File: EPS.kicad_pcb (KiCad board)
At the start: 6 copper layers, 90.2 x 95.9 mm, 1 part

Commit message: progress on switch sheet
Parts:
- added C1101: 1uF, Capacitor_SMD:C_0603_1608Metric_Pad1.08x0.95mm_HandSolder, F.Cu at (64.4, 59.4)
- added C1102: 1uF, Capacitor_SMD:C_0603_1608Metric_Pad1.08x0.95mm_HandSolder, F.Cu at (64.7, 66.5)
- added C1103: 1uF, Capacitor_SMD:C_0603_1608Metric_Pad1.08x0.95mm_HandSolder, F.Cu at (67.7, 65.5)
- added C1104: 1uF, Capacitor_SMD:C_0603_1608Metric_Pad1.08x0.95mm_HandSolder, F.Cu at (67.7, 58.2)
- added C1105: 100nF, Capacitor_SMD:C_0603_1608Metric_Pad1.08x0.95mm_HandSolder, F.Cu at (64.4, 62.8)
- added C1106: 100nF, Capacitor_SMD:C_0603_1608Metric_Pad1.08x0.95mm_HandSolder, F.Cu at (64.6, 70.1)
- added C1301: 1uF, Capacitor_SMD:C_0603_1608Metric_Pad1.08x0.95mm_HandSolder, F.Cu at (41.0, 75.9)
- added C1302: 1uF, Capacitor_SMD:C_0603_1608Metric_Pad1.08x0.95mm_HandSolder, F.Cu at (41.0, 78.5)
- added C1303: 1uF, Capacitor_SMD:C_0603_1608Metric_Pad1.08x0.95mm_HandSolder, F.Cu at (41.0, 81.0)
- added C1304: 1uF, Capacitor_SMD:C_0603_1608Metric_Pad1.08x0.95mm_HandSolder, F.Cu at (41.0, 83.5)
- added C1305: 100nF, Capacitor_SMD:C_0603_1608Metric_Pad1.08x0.95mm_HandSolder, F.Cu at (41.0, 86.0)
- added C1306: 100nF, Capacitor_SMD:C_0603_1608Metric_Pad1.08x0.95mm_HandSolder, F.Cu at (41.0, 88.5)
- added C1601: 1uF, Capacitor_SMD:C_0603_1608Metric_Pad1.08x0.95mm_HandSolder, F.Cu at (53.5, 75.9)
- added C1602: 1uF, Capacitor_SMD:C_0603_1608Metric_Pad1.08x0.95mm_HandSolder, F.Cu at (53.5, 78.5)
- added C1603: 1uF, Capacitor_SMD:C_0603_1608Metric_Pad1.08x0.95mm_HandSolder, F.Cu at (53.5, 81.0)
- added C1604: 1uF, Capacitor_SMD:C_0603_1608Metric_Pad1.08x0.95mm_HandSolder, F.Cu at (53.5, 83.5)
- added C1605: 100nF, Capacitor_SMD:C_0603_1608Metric_Pad1.08x0.95mm_HandSolder, F.Cu at (53.5, 86.0)
- added C1606: 100nF, Capacitor_SMD:C_0603_1608Metric_Pad1.08x0.95mm_HandSolder, F.Cu at (53.5, 88.5)
- added C1701: 1uF, Capacitor_SMD:C_0603_1608Metric_Pad1.08x0.95mm_HandSolder, F.Cu at (53.5, 58.9)
- added C1702: 1uF, Capacitor_SMD:C_0603_1608Metric_Pad1.08x0.95mm_HandSolder, F.Cu at (53.5, 61.4)
- added C1703: 1uF, Capacitor_SMD:C_0603_1608Metric_Pad1.08x0.95mm_HandSolder, F.Cu at (53.5, 63.9)
- added C1704: 1uF, Capacitor_SMD:C_0603_1608Metric_Pad1.08x0.95mm_HandSolder, F.Cu at (53.5, 66.4)
- added C1705: 100nF, Capacitor_SMD:C_0603_1608Metric_Pad1.08x0.95mm_HandSolder, F.Cu at (53.5, 68.9)
- added C1706: 100nF, Capacitor_SMD:C_0603_1608Metric_Pad1.08x0.95mm_HandSolder, F.Cu at (53.5, 71.4)
- added C2801: 1uF, Capacitor_SMD:C_0603_1608Metric_Pad1.08x0.95mm_HandSolder, F.Cu at (41.0, 58.9)
- added C2802: 1uF, Capacitor_SMD:C_0603_1608Metric_Pad1.08x0.95mm_HandSolder, F.Cu at (41.0, 61.4)
- added C2803: 1uF, Capacitor_SMD:C_0603_1608Metric_Pad1.08x0.95mm_HandSolder, F.Cu at (41.0, 63.9)
- added C2804: 1uF, Capacitor_SMD:C_0603_1608Metric_Pad1.08x0.95mm_HandSolder, F.Cu at (41.0, 66.4)
- added C2805: 100nF, Capacitor_SMD:C_0603_1608Metric_Pad1.08x0.95mm_HandSolder, F.Cu at (41.0, 68.9)
- added C2806: 100nF, Capacitor_SMD:C_0603_1608Metric_Pad1.08x0.95mm_HandSolder, F.Cu at (41.0, 71.4)
- added U1101: MCP1703Ax-400xxMB, Package_TO_SOT_SMD:SOT-89-3, F.Cu at (68.3, 61.7)
- added U1102: MCP1703Ax-400xxMB, Package_TO_SOT_SMD:SOT-89-3, F.Cu at (68.5, 68.9)
- added U1301: MCP1703Ax-400xxMB, Package_TO_SOT_SMD:SOT-89-3, F.Cu at (46.5, 77.8)
- added U1302: MCP1703Ax-400xxMB, Package_TO_SOT_SMD:SOT-89-3, F.Cu at (46.5, 83.9)
- added U1601: MCP1703Ax-400xxMB, Package_TO_SOT_SMD:SOT-89-3, F.Cu at (59.0, 77.8)
- added U1602: MCP1703Ax-400xxMB, Package_TO_SOT_SMD:SOT-89-3, F.Cu at (59.0, 83.9)
- added U1701: MCP1703Ax-400xxMB, Package_TO_SOT_SMD:SOT-89-3, F.Cu at (59.0, 60.7)
- added U1702: MCP1703Ax-400xxMB, Package_TO_SOT_SMD:SOT-89-3, F.Cu at (59.0, 66.8)
- added U2801: MCP1703Ax-400xxMB, Package_TO_SOT_SMD:SOT-89-3, F.Cu at (46.5, 60.7)
- added U2802: MCP1703Ax-400xxMB, Package_TO_SOT_SMD:SOT-89-3, F.Cu at (46.5, 66.8)
- added U801: MSP430F5507IRGZ, Package_DFN_QFN:Texas_RGZ0048A_VQFN-48-1EP_7x7mm_P0.5mm_EP5.15x5.15mm, F.Cu at (68.3, 128.4)

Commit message: specified design
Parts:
- removed C1101, C1102, C1103, C1104, C1301, C1302, C1303, C1304, C1601, C1602, C1603, C1604, C1701, C1702, C1703, C1704, C2801, C2802, C2803, C2804: 1uF, Capacitor_SMD:C_0603_1608Metric_Pad1.08x0.95mm_HandSolder
- removed C1105, C1106, C1305, C1306, C1605, C1606, C1705, C1706, C2805, C2806: 100nF, Capacitor_SMD:C_0603_1608Metric_Pad1.08x0.95mm_HandSolder
- removed U1101, U1102, U1301, U1302, U1601, U1602, U1701, U1702, U2801, U2802: MCP1703Ax-400xxMB, Package_TO_SOT_SMD:SOT-89-3
- removed U801: MSP430F5507IRGZ, Package_DFN_QFN:Texas_RGZ0048A_VQFN-48-1EP_7x7mm_P0.5mm_EP5.15x5.15mm
- added H102: MountingHole, MountingHole:MountingHole_3.2mm_M3_Pad_Via, F.Cu at (160.0, 132.9)
- added H103: MountingHole, MountingHole:MountingHole_3.2mm_M3_Pad_Via, F.Cu at (240.0, 132.9)
- added H104: MountingHole, MountingHole:MountingHole_3.2mm_M3_Pad_Via, F.Cu at (163.9, 47.1)
- added H5901: Conn_02x26_Odd_Even, Connector_PinSocket_2.54mm:PinSocket_2x26_P2.54mm_Vertical, F.Cu at (168.9, 47.1)
- added H5902: Conn_02x26_Odd_Even, Connector_PinSocket_2.54mm:PinSocket_2x26_P2.54mm_Vertical, F.Cu at (168.9, 52.3)
- added PCB101: PCB Outline, Outlines:SPACEMANIC_V1c, F.Cu at (200.0, 90.0)
- added PCB102: PCB Outline, Outlines:SPACEMANIC_V1c, F.Cu at (84.6, 90.0)
- added PCB103: PCB Outline, Outlines:SPACEMANIC_V1c, F.Cu at (82.6, 200.1)
- added R_RX_5901: 0R, Resistor_SMD:R_0603_1608Metric_Pad0.98x0.95mm_HandSolder, F.Cu at (310.4, 164.3)
- added R_TX_5901: 0R, Resistor_SMD:R_0603_1608Metric_Pad0.98x0.95mm_HandSolder, F.Cu at (312.2, 164.3)
- H101: value PCB Outline -> MountingHole; footprint Outlines:SPACEMANIC_V1c -> MountingHole:MountingHole_3.2mm_M3_Pad_Via
- moved H101 103.0 mm to (237.5, 47.1)
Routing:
- net /Interface/RX: track 0.00 -> 4.78 mm
- net /Interface/RxD: track 0.00 -> 4.34 mm
- net /Interface/TX: track 0.00 -> 2.79 mm
- net /Interface/TxD: track 0.00 -> 2.39 mm
- added copper zone on In1.Cu, net GND
- added copper zone on In4.Cu, net GND
- added copper zone on B.Cu, net SHIELD
- added copper zone on F.Cu, net SHIELD
- added copper zone on In3.Cu, net VBUS
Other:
- board size 90.2 x 95.9 mm -> 90 x 95.8 mm

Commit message: added second AMUX and housekeeping
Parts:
- added H105: MountingHole, MountingHole:MountingHole_3.2mm_M3_Pad_Via, F.Cu at (48.5, 47.1)
- added H106: MountingHole, MountingHole:MountingHole_3.2mm_M3_Pad_Via, F.Cu at (44.6, 132.9)
- added H107: MountingHole, MountingHole:MountingHole_3.2mm_M3_Pad_Via, F.Cu at (124.6, 132.9)
- added H108: MountingHole, MountingHole:MountingHole_3.2mm_M3_Pad_Via, F.Cu at (122.1, 47.1)
- added PCB104: PCB Outline, Outlines:SPACEMANIC_V1c, F.Cu at (-181.4, 64.0)
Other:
- board size 90 x 95.8 mm -> 205.4 x 95.8 mm

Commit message: added RS422, housekeeping
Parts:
- moved PCB104 303.9 mm to (99.7, -51.3)
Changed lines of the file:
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@@
 	(footprint "Outlines:SPACEMANIC_V1c"
 		(layer "F.Cu")
-		(at -181.4075 64.05)
+		(at 99.7 -51.3)
 		(property "Reference" "PCB104"
 			(at 0 -0.5 0)

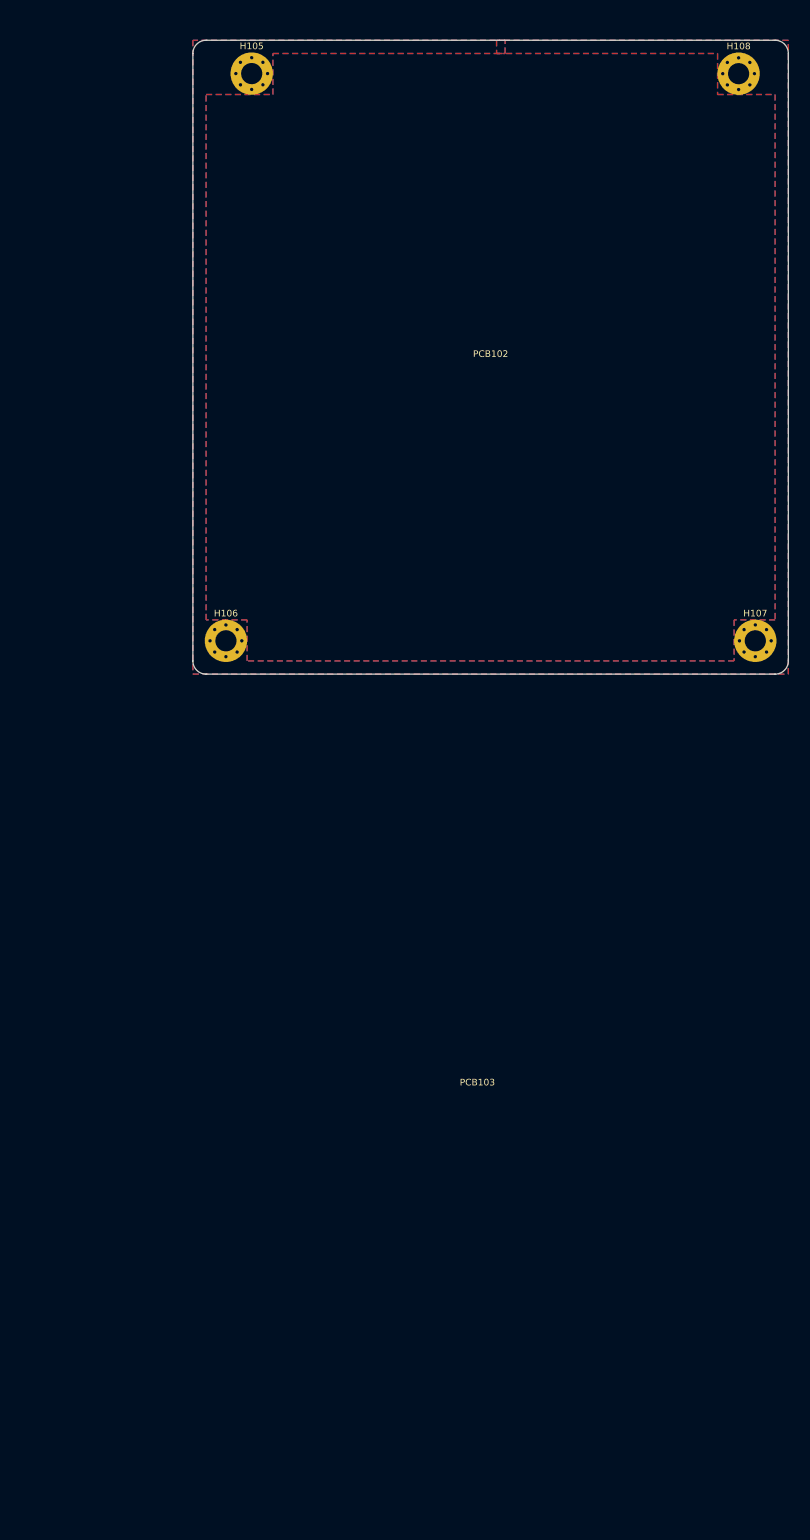
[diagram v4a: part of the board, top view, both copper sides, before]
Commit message: updated battery pack module; updated solar inputs module
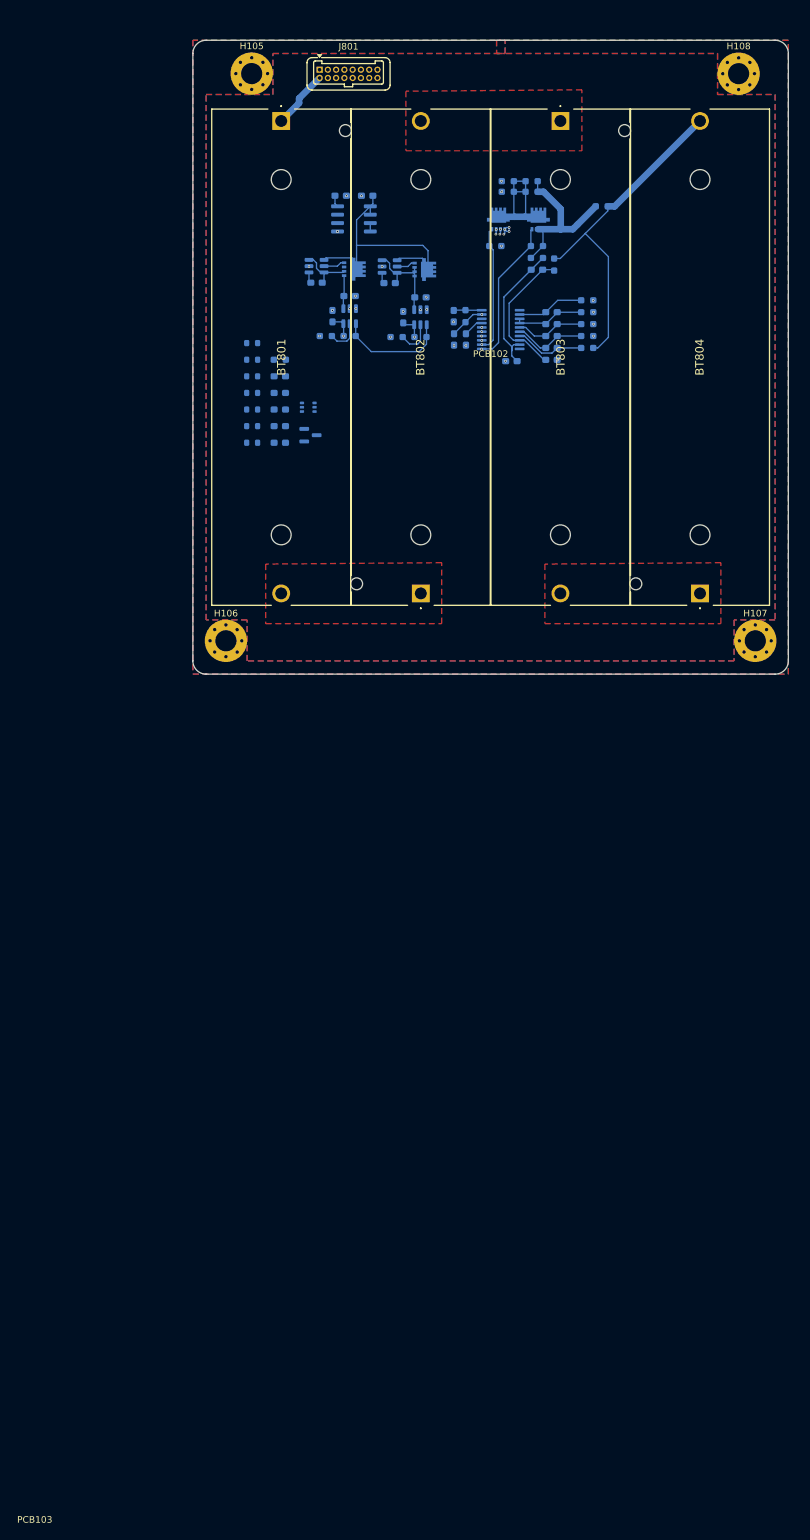
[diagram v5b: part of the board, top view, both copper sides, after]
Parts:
- added BT801: Battery_Cell, Outlines:BHC186501P-li-ion, F.Cu at (53.0, 54.3)
- added BT802: Battery_Cell, Outlines:BHC186501P-li-ion, F.Cu at (74.0, 125.7)
- added BT803: Battery_Cell, Outlines:BHC186501P-li-ion, F.Cu at (95.2, 54.3)
- added BT804: Battery_Cell, Outlines:BHC186501P-li-ion, F.Cu at (116.2, 125.7)
- added C2701: 1u, Capacitor_SMD:C_0603_1608Metric_Pad1.08x0.95mm_HandSolder, B.Cu at (52.7, 102.9)
- added C2702: 10n, Capacitor_SMD:C_0603_1608Metric_Pad1.08x0.95mm_HandSolder, B.Cu at (52.7, 100.4)
- added C2703: 10u, Capacitor_SMD:C_0603_1608Metric_Pad1.08x0.95mm_HandSolder, B.Cu at (52.7, 97.9)
- added C2704: 3.3n, Capacitor_SMD:C_0603_1608Metric_Pad1.08x0.95mm_HandSolder, B.Cu at (52.7, 95.4)
- added C2705: 10n, Capacitor_SMD:C_0603_1608Metric_Pad1.08x0.95mm_HandSolder, B.Cu at (52.7, 92.9)
- added C3301: 1u, Capacitor_SMD:C_0603_1608Metric_Pad1.08x0.95mm_HandSolder, B.Cu at (69.3, 78.8)
- added C3302: 1u, Capacitor_SMD:C_0603_1608Metric_Pad1.08x0.95mm_HandSolder, B.Cu at (58.3, 78.7)
- added C3303: 1u, Capacitor_SMD:C_0603_1608Metric_Pad1.08x0.95mm_HandSolder, B.Cu at (65.9, 65.6)
- added C3304: 1u, Capacitor_SMD:C_0603_1608Metric_Pad1.08x0.95mm_HandSolder, B.Cu at (61.9, 65.6)
- added C3501: 1u, Capacitor_SMD:C_0603_1608Metric_Pad1.08x0.95mm_HandSolder, B.Cu at (71.4, 84.0)
- added C3502: 1u, Capacitor_SMD:C_0603_1608Metric_Pad1.08x0.95mm_HandSolder, B.Cu at (60.7, 83.8)
- added C3503: 1u, Capacitor_SMD:C_0603_1608Metric_Pad1.08x0.95mm_HandSolder, B.Cu at (74.0, 81.0)
- added C3504: 1u, Capacitor_SMD:C_0603_1608Metric_Pad1.08x0.95mm_HandSolder, B.Cu at (63.3, 80.8)
- added C801: 1uF, Capacitor_SMD:C_0603_1608Metric_Pad1.08x0.95mm_HandSolder, B.Cu at (93.8, 83.2)
- added C802: 1uF, Capacitor_SMD:C_0603_1608Metric_Pad1.08x0.95mm_HandSolder, B.Cu at (93.8, 85.0)
- added C803: 1uF, Capacitor_SMD:C_0603_1608Metric_Pad1.08x0.95mm_HandSolder, B.Cu at (93.8, 86.8)
- added C804: 1uF, Capacitor_SMD:C_0603_1608Metric_Pad1.08x0.95mm_HandSolder, B.Cu at (93.8, 88.6)
- added C805: 1uF, Capacitor_SMD:C_0603_1608Metric_Pad1.08x0.95mm_HandSolder, B.Cu at (80.9, 87.3)
- added C806: C_Small, Capacitor_SMD:C_0603_1608Metric_Pad1.08x0.95mm_HandSolder, B.Cu at (79.1, 87.3)
- added C807: 1uF, Capacitor_SMD:C_0603_1608Metric_Pad1.08x0.95mm_HandSolder, B.Cu at (93.8, 90.4)
- added C808: 1uF, Capacitor_SMD:C_0603_1608Metric_Pad1.08x0.95mm_HandSolder, B.Cu at (91.6, 76.8)
- added C809: C_Small, Capacitor_SMD:C_0603_1608Metric_Pad1.08x0.95mm_HandSolder, B.Cu at (79.0, 83.8)
- added C810: 1uF, Capacitor_SMD:C_0603_1608Metric_Pad1.08x0.95mm_HandSolder, B.Cu at (87.7, 90.6)
- added J801: Battery_1, Connector_Harwin:Harwin_Gecko-G125-FVX1605L0X_2x08_P1.25mm_Vertical, F.Cu at (58.8, 46.5)
- added Q2701: IRLML5103, Package_TO_SOT_SMD:SOT-23, B.Cu at (57.4, 101.8)
- added Q3301: NMOS, Outlines:NVTFS5116PLTWG, B.Cu at (74.5, 76.8)
- added Q3302: NMOS, Outlines:NVTFS5116PLTWG, B.Cu at (63.9, 76.7)
- added Q801: NMOS, Outlines:NVTFS5116PLTWG, B.Cu at (91.8, 69.2)
- added Q802: NMOS, Outlines:NVTFS5116PLTWG, B.Cu at (85.8, 69.2)
- added R2701: 100k, Resistor_SMD:R_0603_1608Metric_Pad0.98x0.95mm_HandSolder, B.Cu at (52.7, 90.4)
- added R2702: 10K, Resistor_SMD:R_0603_1608Metric, B.Cu at (48.6, 102.9)
- added R2703: 39k, Resistor_SMD:R_0603_1608Metric, B.Cu at (48.6, 100.4)
- added R2704: 22R, Resistor_SMD:R_0603_1608Metric, B.Cu at (48.6, 97.9)
- added R2705: 100R, Resistor_SMD:R_0603_1608Metric, B.Cu at (48.6, 95.4)
- added R2706: 1k, Resistor_SMD:R_0603_1608Metric, B.Cu at (48.6, 92.9)
- added R2707: 150R, Resistor_SMD:R_0603_1608Metric, B.Cu at (48.6, 90.4)
- added R2708: 2k49, Resistor_SMD:R_0603_1608Metric, B.Cu at (48.6, 87.9)
- added R3501: 100k, Resistor_SMD:R_0603_1608Metric_Pad0.98x0.95mm_HandSolder, B.Cu at (74.0, 87.0)
- added R3502: 100k, Resistor_SMD:R_0603_1608Metric_Pad0.98x0.95mm_HandSolder, B.Cu at (63.3, 86.8)
- added R3503: R_Small, Resistor_SMD:R_0603_1608Metric_Pad0.98x0.95mm_HandSolder, B.Cu at (70.4, 87.0)
- added R3504: R_Small, Resistor_SMD:R_0603_1608Metric_Pad0.98x0.95mm_HandSolder, B.Cu at (59.7, 86.8)
- added R801: R_Small, Resistor_SMD:R_0603_1608Metric_Pad0.98x0.95mm_HandSolder, B.Cu at (99.2, 81.4)
- added R802: R_Small, Resistor_SMD:R_0603_1608Metric_Pad0.98x0.95mm_HandSolder, B.Cu at (99.2, 83.2)
- added R803: R_Small, Resistor_SMD:R_0603_1608Metric_Pad0.98x0.95mm_HandSolder, B.Cu at (99.2, 85.0)
- added R804: R_Small, Resistor_SMD:R_0603_1608Metric_Pad0.98x0.95mm_HandSolder, B.Cu at (99.2, 86.8)
- added R805: R_Small, Resistor_SMD:R_0603_1608Metric_Pad0.98x0.95mm_HandSolder, B.Cu at (99.2, 88.6)
- added R806: R_Small, Resistor_SMD:R_0603_1608Metric_Pad0.98x0.95mm_HandSolder, B.Cu at (94.2, 76.0)
- added R807: R_Small, Resistor_SMD:R_0603_1608Metric_Pad0.98x0.95mm_HandSolder, B.Cu at (101.4, 67.2)
- added R808: R_Small, Resistor_SMD:R_0603_1608Metric_Pad0.98x0.95mm_HandSolder, B.Cu at (80.8, 83.8)
- added R809: R_Small, Resistor_SMD:R_0603_1608Metric_Pad0.98x0.95mm_HandSolder, B.Cu at (91.6, 75.0)
- added R810: R_Small, Resistor_SMD:R_0603_1608Metric_Pad0.98x0.95mm_HandSolder, B.Cu at (91.6, 73.2)
- added R811: 0R, Resistor_SMD:R_0603_1608Metric_Pad0.98x0.95mm_HandSolder, B.Cu at (90.8, 63.4)
- added R812: 0R, Resistor_SMD:R_0603_1608Metric_Pad0.98x0.95mm_HandSolder, B.Cu at (90.8, 65.0)
- added R813: 0R, Resistor_SMD:R_0603_1608Metric_Pad0.98x0.95mm_HandSolder, B.Cu at (87.2, 63.4)
- added R814: 0R, Resistor_SMD:R_0603_1608Metric_Pad0.98x0.95mm_HandSolder, B.Cu at (87.2, 65.0)
- added R815: R_Small, Resistor_SMD:R_0603_1608Metric_Pad0.98x0.95mm_HandSolder, B.Cu at (85.3, 73.2)
- added U2701: ADA4807-1, Package_TO_SOT_SMD:SOT-363_SC-70-6, B.Cu at (57.0, 97.6)
- added U3301: LM74700, Package_TO_SOT_SMD:SOT-23-6, B.Cu at (69.3, 76.3)
- added U3302: LM74700, Package_TO_SOT_SMD:SOT-23-6, B.Cu at (58.3, 76.2)
- added U3303: TMCS1101A2UQDT, Package_SO:SOIC-8_3.9x4.9mm_P1.27mm, B.Cu at (63.9, 69.1)
- added U3501: AP22653AW6-7, Package_TO_SOT_SMD:SOT-23-6, B.Cu at (74.0, 84.0)
- added U3502: AP22653AW6-7, Package_TO_SOT_SMD:SOT-23-6, B.Cu at (63.3, 83.8)
- added U801: BQ76920PW, Package_SO:TSSOP-20_4.4x6.5mm_P0.65mm, B.Cu at (86.1, 85.8)
- moved PCB103 94.0 mm to (15.7, 266.2)
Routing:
- net /Battery_Input_1/BATT_3: track 0.00 -> 53.3 mm, vias 0 -> 1
- net /Battery_Input_1/BATT_0: track 0.00 -> 51.2 mm
- net /Battery_Input_1/BATT_1: track 0.00 -> 42.7 mm, vias 0 -> 1
- net Net-(Q3301-D): track 0.00 -> 42.3 mm
- net /Battery_Input_1/BATT_2: track 0.00 -> 34.5 mm, vias 0 -> 1
- net Net-(Q801-D): track 0.00 -> 27.5 mm
- net Net-(Q801-S): track 0.00 -> 26.2 mm
- net /Battery_Input_1/DSG: track 0.00 -> 22.2 mm, vias 0 -> 1
- net /Battery_Input_1/Pack: track 0.00 -> 21.6 mm, vias 0 -> 4
- net /Battery_Input_1/SRN: track 0.00 -> 21.3 mm
- net /Battery_Input_1/SRP: track 0.00 -> 20.9 mm
- net /Battery_Input_1/CHG: track 0.00 -> 19.2 mm, vias 0 -> 1
- net /Battery_Input_1/Switch_Batt_Heater/~{ALERT}: track 0.00 -> 17.0 mm
- net /Battery_Input_1/Switch_Batt_Heater/Switch_element/VOUT1: track 0.00 -> 14.3 mm
- net /Battery_Input_1/Switch_Batt_Heater/Switch_element/VOUT2: track 0.00 -> 13.3 mm
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- added copper zone on F.Cu, net /Battery_Input_1/BATT_1
- added copper zone on In3.Cu, net /Battery_Input_1/BATT_1
- added copper zone on F.Cu, net /Battery_Input_1/BATT_2
- added copper zone on In3.Cu, net /Battery_Input_1/BATT_2
- added copper zone on F.Cu, net /Battery_Input_1/BATT_3
- added copper zone on In3.Cu, net /Battery_Input_1/BATT_3
- added copper zone on In3.Cu, net /Battery_Input_1/Pack
